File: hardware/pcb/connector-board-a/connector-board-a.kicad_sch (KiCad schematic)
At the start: 2 parts, among them J1 DE9_Pins, J2 Conn_01x09_Pin

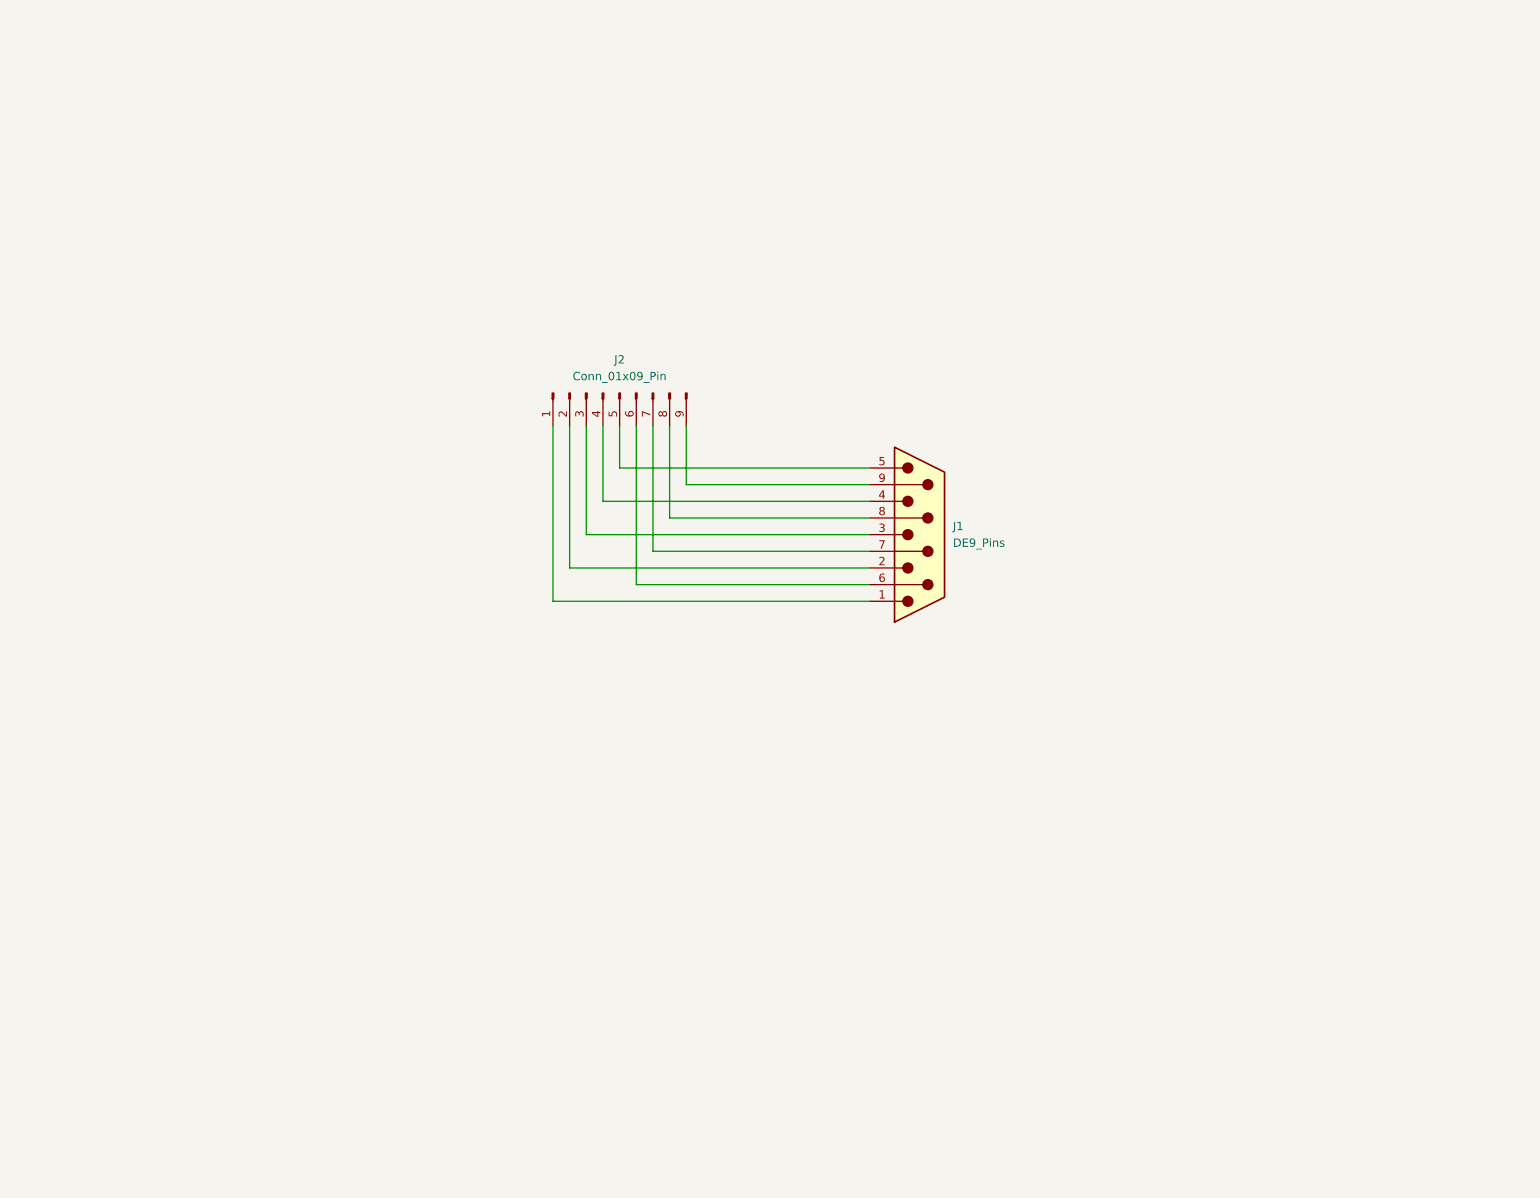
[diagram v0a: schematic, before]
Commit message: Updated connector A board to rev 1.1
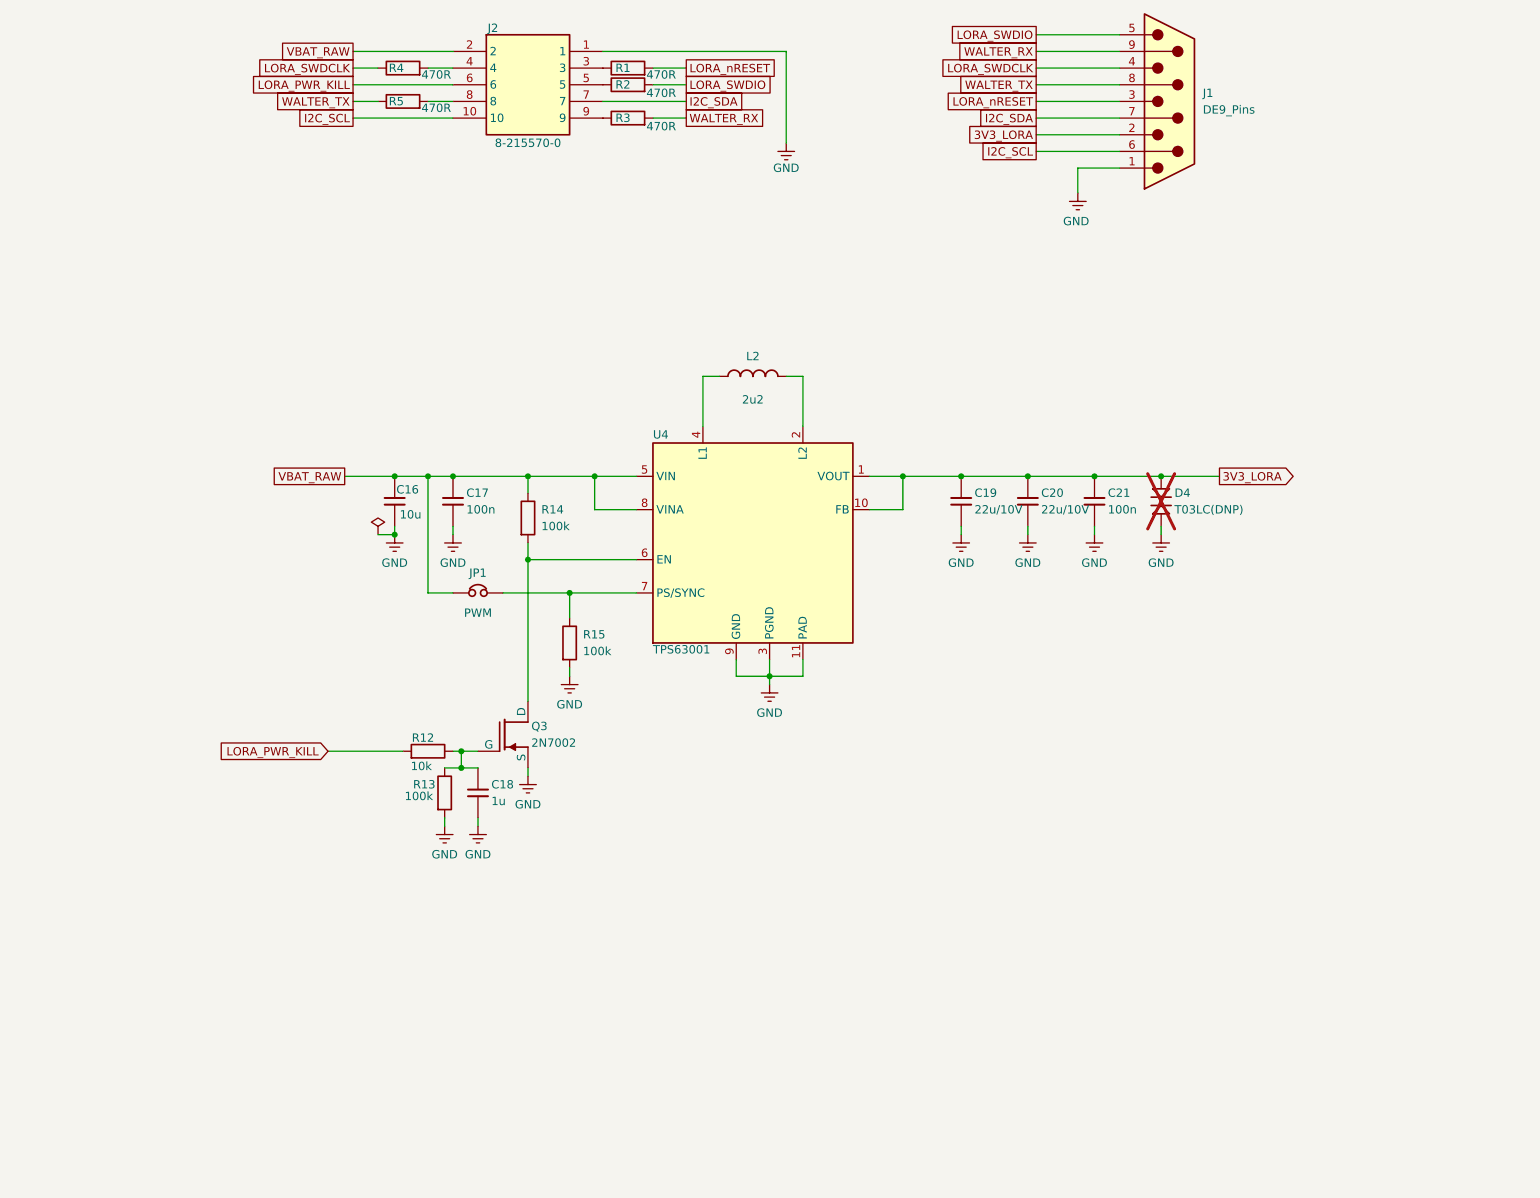
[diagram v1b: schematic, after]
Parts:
- removed J2: Conn_01x09_Pin, TwinOak platform footprints:82155700, symbol Connector:Conn_01x09_Pin
- added C16: 10u, Capacitor_SMD:C_0805_2012Metric, symbol lora3v3:C_V
- added C17, C21: 100n, Capacitor_SMD:C_0603_1608Metric, symbol lora3v3:C_V
- added C18: 1u, Capacitor_SMD:C_0603_1608Metric, symbol lora3v3:C_V
- added C19, C20: 22u/10V, Capacitor_SMD:C_0805_2012Metric, symbol lora3v3:C_V
- added D4: T03LC(DNP), Diode_SMD:D_SOD-323, symbol lora3v3:TVS_V
- added J2: 8-215570-0, TwinOak platform footprints:82155700, symbol 8-215570-0:8-215570-0
- added JP1: PWM, Jumper:SolderJumper-2_P1.3mm_Open_RoundedPad1.0x1.5mm, symbol lora3v3:JUMPER_H
- added L2: 2u2, Inductor_SMD:L_Coilcraft_LPS4018, symbol lora3v3:L_H
- added Q3: 2N7002, Package_TO_SOT_SMD:SOT-23, symbol lora3v3:NMOS
- added R1, R2, R3, R4, R5: 470R, Resistor_SMD:R_0805_2012Metric, symbol Device:R
- added R12: 10k, Resistor_SMD:R_0805_2012Metric, symbol lora3v3:R_H
- added R13, R14, R15: 100k, Resistor_SMD:R_0805_2012Metric, symbol lora3v3:R_V
- added U4: TPS63001, Package_SON:Texas_DRC0010J, symbol lora3v3:TPS63001
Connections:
- net GND: now reaches J1.1
- net GND: now also C16.2, C17.2, C18.2, C19.2, C20.2, C21.2, D4.2, J2.1, Q3.2 (S), R13.2, R15.2, U4.11 (PAD), U4.3 (PGND), U4.9 (GND)
- net 3V3_LORA: now reaches J1.2
- net 3V3_LORA: now also C19.1, C20.1, C21.1, D4.1, U4.1 (VOUT), U4.10 (FB)
- net LORA_nRESET: now reaches J1.3
- net LORA_nRESET: now also R1.2
- net LORA_SWDCLK: now reaches J1.4
- net LORA_SWDCLK: now also R4.1
- net LORA_SWDIO: now reaches J1.5
- net LORA_SWDIO: now also R2.2
- net I2C_SCL: now reaches J1.6
- net I2C_SCL: now also J2.10
- net I2C_SDA: now reaches J1.7
- net I2C_SDA: now also J2.7
- net WALTER_TX: now reaches J1.8
- net WALTER_TX: now also R5.1
- net WALTER_RX: now reaches J1.9
- net WALTER_RX: now also R3.2
- new net: J2.9, R3.1
- new net: C18.1, Q3.1 (G), R12.2, R13.1
- new net: Q3.3 (D), R14.2, U4.6 (EN)
- new net: JP1.2, R15.1, U4.7 (PS/SYNC)
- new net: J2.4, R4.2
- new net: J2.8, R5.2
- new net: L2.1, U4.4 (L1)
- new net: L2.2, U4.2 (L2)
- new net: J2.3, R1.1
- new net: J2.5, R2.1
- new net LORA_PWR_KILL: J2.6, R12.1
- new net VBAT_RAW: C16.1, C17.1, J2.2, JP1.1, R14.1, U4.5 (VIN), U4.8 (VINA)
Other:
- moved on the sheet: J1

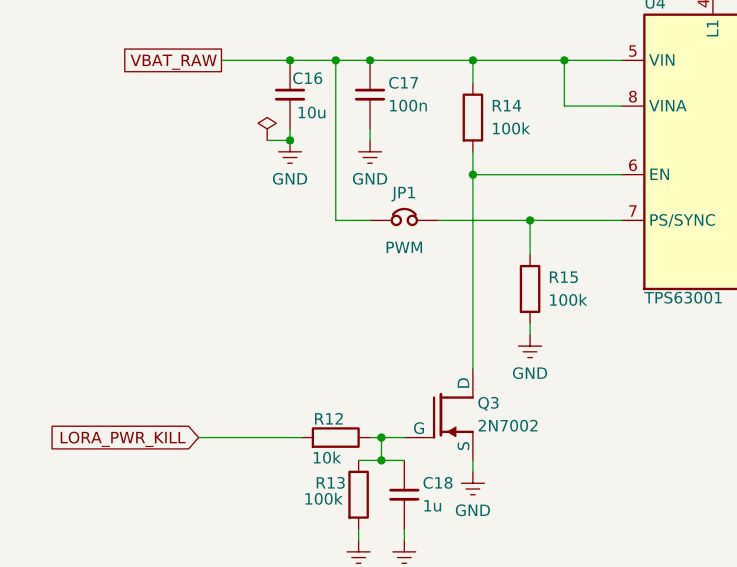
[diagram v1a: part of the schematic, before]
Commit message: Added missing description
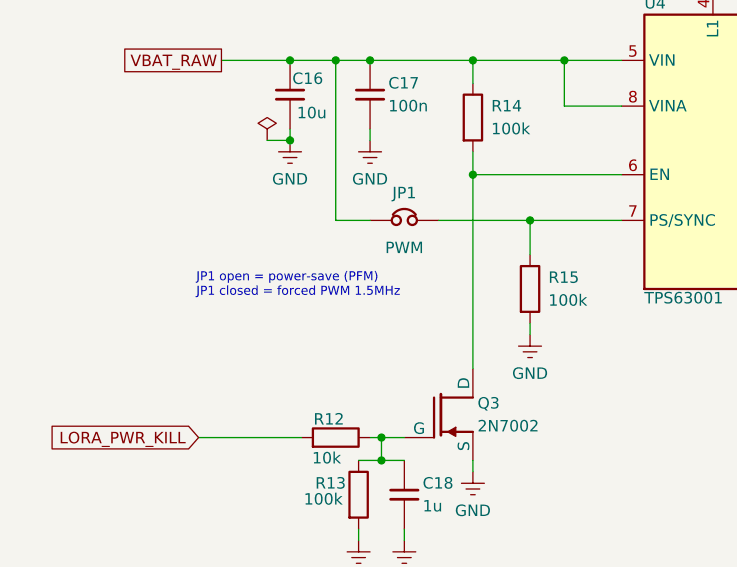
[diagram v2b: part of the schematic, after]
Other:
- note added: "JP1 open = power-save (PFM) JP1 closed = forced PWM 1.5MHz"
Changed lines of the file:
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@@
 	(generator_version "10.0")
 	(paper "A4")
+	(text "JP1 open = power-save (PFM)\nJP1 closed = forced PWM 1.5MHz"
+		(exclude_from_sim no)
+		(at 82.296 120.396 0)
+		(effects
+			(font
+				(size 1 1)
+			)
+			(justify left bottom)
+		)
+	)
 	(junction
 		(at 179.07 93.98)

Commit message: Cleanup
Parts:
- removed JP1: PWM, Jumper:SolderJumper-2_P1.3mm_Open_RoundedPad1.0x1.5mm, symbol lora3v3:JUMPER_H
- added JP1: PWM_MODE, Connector_PinHeader_2.54mm:PinHeader_1x02_P2.54mm_Vertical, symbol Connector:Conn_01x02_Pin
- J2: footprint TwinOak platform footprints:82155700 -> TwinOak:82155700; symbol 8-215570-0:8-215570-0 -> TwinOak:8-215570-0
- U4: symbol lora3v3:TPS63001 -> TwinOak:TPS63001
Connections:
- net VBAT_RAW: now also JP1.1 (Pin_1)
- net PS_SYNC: now reaches R15.1, U4.7 (PS/SYNC)
- net PS_SYNC: now also JP1.2 (Pin_2)

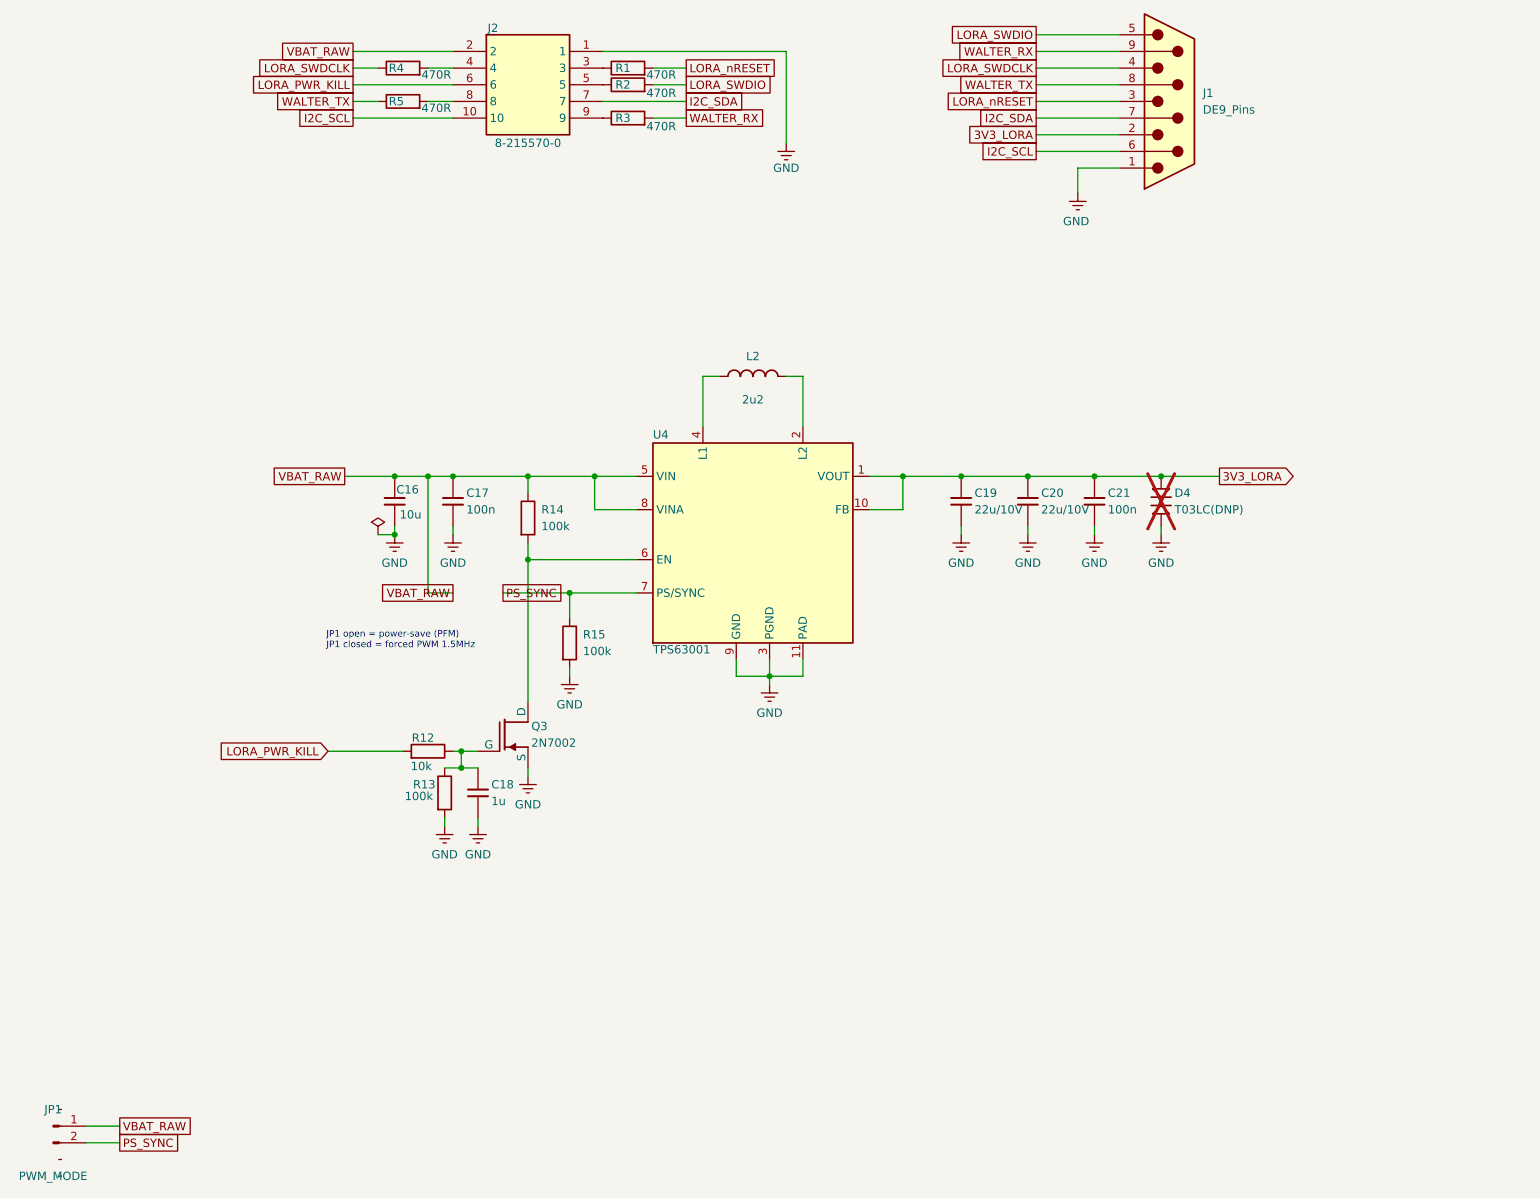
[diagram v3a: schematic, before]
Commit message: Routing of connector b board
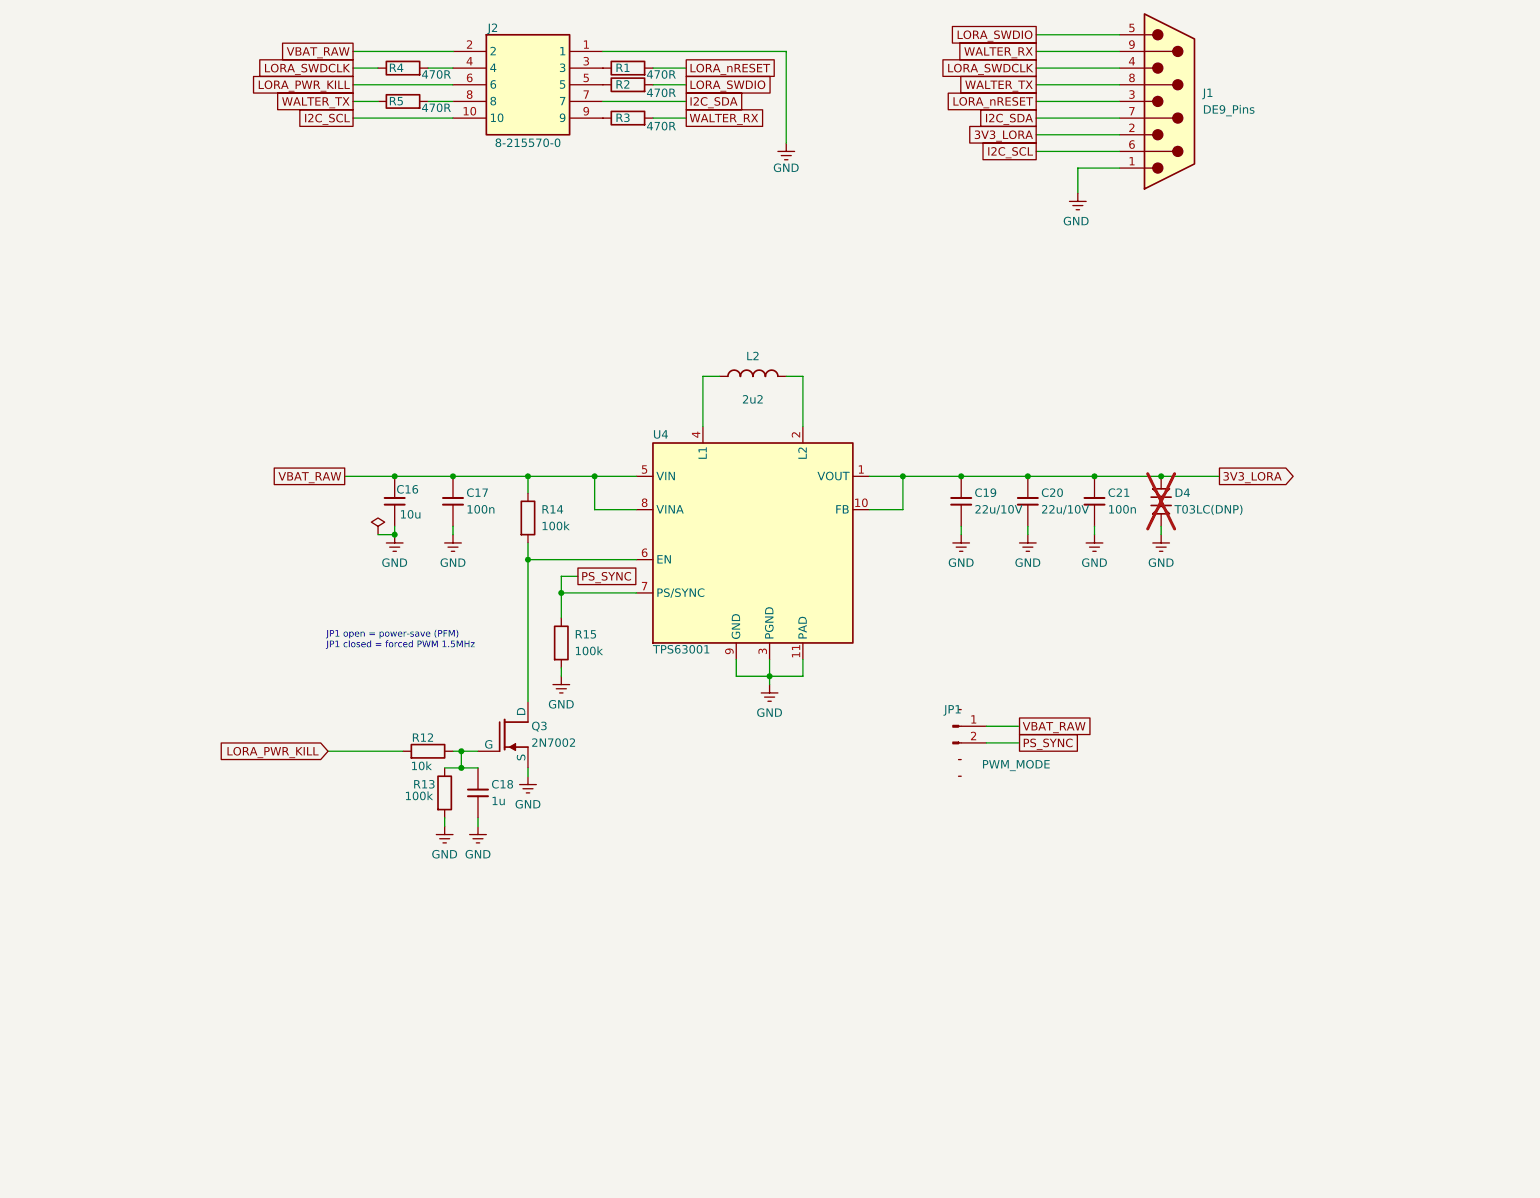
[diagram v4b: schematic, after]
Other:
- moved on the sheet: JP1, R15

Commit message: Misc changes
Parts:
- R13, R14, R15: LCSC Part # C17407 -> C149504
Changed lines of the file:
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@@
 			)
 		)
-		(property "LCSC Part #" "C17407"
+		(property "LCSC Part #" "C149504"
 			(at 118.11 119.38 0)
 			(hide yes)
@@
 			)
 		)
-		(property "LCSC Part #" "C17407"
+		(property "LCSC Part #" "C149504"
 			(at 100.33 142.24 0)
 			(hide yes)
@@
 			)
 		)
-		(property "LCSC Part #" "C17407"
+		(property "LCSC Part #" "C149504"
 			(at 113.03 100.33 0)
 			(hide yes)

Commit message: Misc minor updates for production of pcbs
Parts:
- D4, J1, J2, JP1: now left out of the parts list
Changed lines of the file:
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@@
 		(body_style 1)
 		(exclude_from_sim no)
-		(in_bom yes)
-		(on_board yes)
-		(in_pos_files yes)
+		(in_bom no)
+		(on_board yes)
+		(in_pos_files no)
 		(dnp yes)
 		(property "Reference" "D4"
@@
 		(body_style 1)
 		(exclude_from_sim no)
-		(in_bom yes)
-		(on_board yes)
-		(in_pos_files yes)
+		(in_bom no)
+		(on_board yes)
+		(in_pos_files no)
 		(dnp no)
 		(fields_autoplaced yes)
@@
 		(body_style 1)
 		(exclude_from_sim no)
-		(in_bom yes)
-		(on_board yes)
-		(in_pos_files yes)
+		(in_bom no)
+		(on_board yes)
+		(in_pos_files no)
 		(dnp no)
 		(property "Reference" "J2"
@@
 		(body_style 1)
 		(exclude_from_sim no)
-		(in_bom yes)
-		(on_board yes)
-		(in_pos_files yes)
+		(in_bom no)
+		(on_board yes)
+		(in_pos_files no)
 		(dnp no)
 		(property "Reference" "JP1"
